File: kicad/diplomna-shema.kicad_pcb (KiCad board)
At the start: 2 copper layers, 99.8 x 79.1 mm, 20 parts, among them J1 Power input 12VDC, J7 micro switch, M2 Motor_Servo, U1 TCS3200, U2 TCRT5000, U3 HC-SR04, U4 LCD-TFT-2.8inch, U5 HX711

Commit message: Add files via upload
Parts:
- added ?: , , F.Cu at (32.6, 25.6)
- added ?: , , F.Cu at (128.4, 100.7)
- added ?: , , F.Cu at (128.4, 25.6)
- added ?: , , F.Cu at (32.6, 100.7)
- moved REF** 7.13 mm to (45.7, 99.2), turned to -90 degrees
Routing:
- net Net-(A1-Pad6): track 15.3 -> 4.42 mm
- net Net-(A1-Pad3): track 12.2 -> 3.26 mm
- net Net-(A2-Pad47): track 126.7 -> 134.1 mm
- net Net-(A2-Pad32): track 87.2 -> 94.1 mm
- net Net-(A2-Pad51): track 19.5 -> 24.7 mm
- net Net-(A1-Pad5): track 9.55 -> 4.42 mm
- net GND: track 282.4 -> 287.3 mm
- net Net-(A2-Pad45): track 154.5 -> 158.3 mm
- net +12V: track 230.8 -> 234.5 mm, vias 0 -> 1
- net Net-(A2-Pad24): track 54.7 -> 58.4 mm
- net Net-(A2-Pad37): track 68.0 -> 71.3 mm
- net Net-(A2-Pad26): track 66.4 -> 69.7 mm
- net Net-(A2-Pad35): track 45.0 -> 48.2 mm
- net Net-(A2-PadAD0): track 91.3 -> 94.3 mm
- net Net-(A1-Pad15): track 18.3 -> 21.0 mm
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- removed copper zone on F.Cu, net (none)
- removed copper zone on B.Cu, net GND
- removed copper zone on F.Cu, net GND

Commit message: Add files via upload
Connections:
- U4 pad 10: Net-(R5-Pad2) -> Net-(R3-Pad1)
- U4 pad 7: +3.3V -> Net-(R3-Pad1)
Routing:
- net +3.3V: track 98.0 -> 131.2 mm, vias 1 -> 2
- net Net-(R3-Pad1): track 81.8 -> 91.5 mm
- net Net-(A2-Pad51): track 24.7 -> 27.4 mm
- net +5V: track 216.9 -> 214.3 mm
- net +12V: track 234.5 -> 236.9 mm
- net Net-(A2-PadAD0): track 94.3 -> 92.0 mm
- net Net-(A1-Pad9): track 15.7 -> 18.0 mm
- net GND: track 287.3 -> 288.9 mm
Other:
- board text added: "T_IRG T_DO T_DIN T_CS T_CLK MISO LED SCK MOSI DC RESET CS GND VCC"

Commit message: Add files via upload
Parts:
- added R9: 10kΩ, Resistor_SMD:R_0805_2012Metric, F.Cu at (56.6, 50.9)
- moved R4 2.21 mm to (52.1, 56.8), turned to -90 degrees
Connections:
- R4 pad 1: Net-(A2-Pad39) -> GND
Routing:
- net GND: track 288.9 -> 322.1 mm, vias 2 -> 4
- net +12V: track 236.9 -> 239.0 mm, vias 1 -> 2
- net Net-(A2-Pad39): track 62.7 -> 63.3 mm

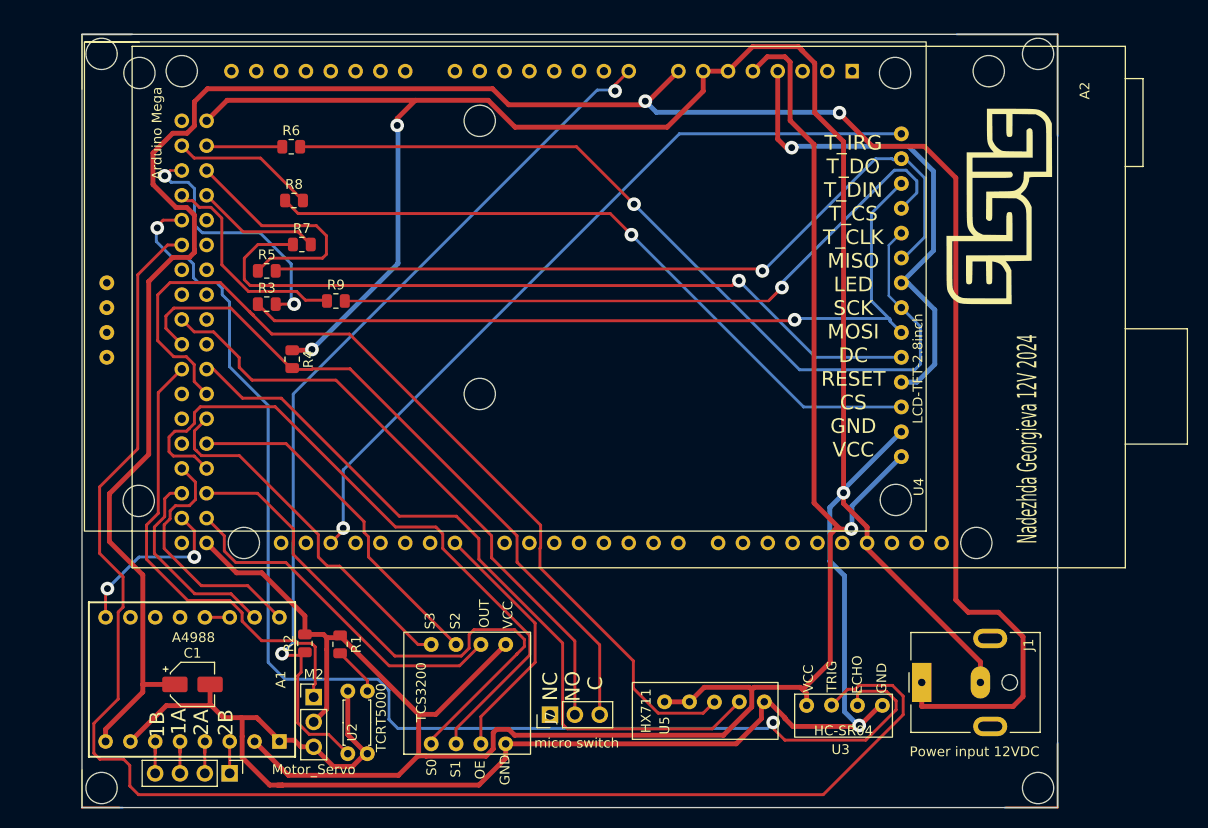
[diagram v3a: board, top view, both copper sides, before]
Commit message: последна версия - корекции по платка и схема, нови 3Dчасти за конструкция със сменен мотор и преправен код
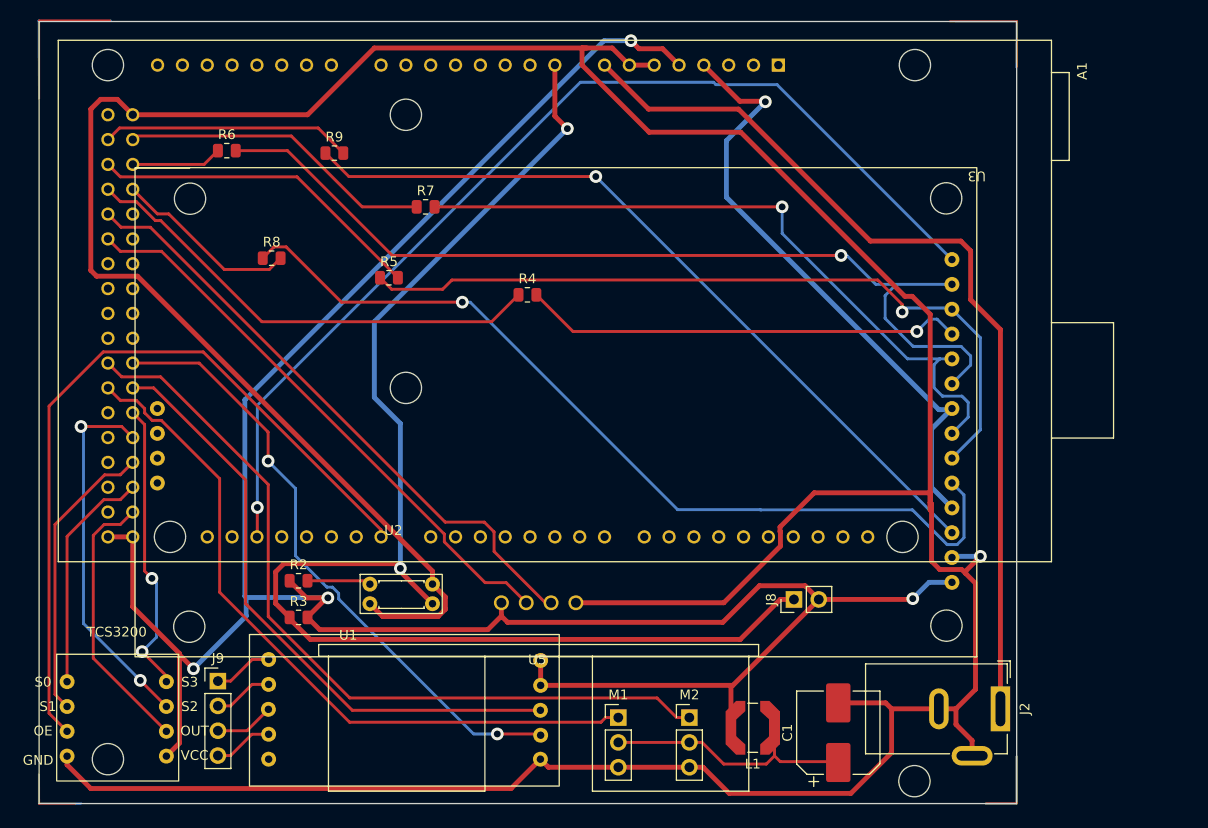
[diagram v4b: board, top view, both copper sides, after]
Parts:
- removed the ? at (32.6, 25.6)
- removed the ? at (128.4, 100.7)
- removed the ? at (128.4, 25.6)
- removed the ? at (32.6, 100.7)
- removed A2: Arduino Mega, Library:arduino_mega2560
- removed J1: Power input 12VDC, Connector_BarrelJack:BarrelJack_CUI_PJ-063AH_Horizontal
- removed J7: micro switch, Connector_PinHeader_2.54mm:PinHeader_1x03_P2.54mm_Vertical
- removed R1: 100Ω, Resistor_SMD:R_0805_2012Metric
- removed REF**: PinHeader_1x04_P2.54mm_Vertical, Connector_PinHeader_2.54mm:PinHeader_1x04_P2.54mm_Vertical
- added ?: , , F.Cu at (33.2, 97.8)
- added ?: , , F.Cu at (115.8, 100.0)
- added J2: Power input 5VDC, Connector_BarrelJack:BarrelJack_GCT_DCJ200-10-A_Horizontal, F.Cu at (124.5, 92.6)
- added J8: PinHeader_1x02_P2.54mm_Vertical, Connector_PinHeader_2.54mm:PinHeader_1x02_P2.54mm_Vertical, F.Cu at (103.4, 81.4)
- added J9: PinHeader_1x04_P2.54mm_Vertical, Connector_PinHeader_2.54mm:PinHeader_1x04_P2.54mm_Vertical, F.Cu at (44.5, 89.8)
- added L1: L, Inductor_SMD:L_Coilcraft_LPS5030, F.Cu at (99.2, 94.5)
- added M1: Motor_rampa, Connector_PinHeader_2.54mm:PinHeader_1x03_P2.54mm_Vertical, F.Cu at (85.5, 93.5)
- A1: value A4988 -> Arduino Mega; footprint Module:Pololu_Breakout-16_15.2x20.3mm -> Library:arduino_mega2560; moved to F.Cu
- C1: value C_Small -> C; footprint Capacitor_SMD:CP_Elec_4x3 -> Capacitor_SMD:CP_Elec_8x5.4
- M2: value Motor_Servo -> Futuba S3003
- R2: value 10kΩ -> 100Ω
- R4: value 10kΩ -> 10k
- U1: value TCS3200 -> HC-SR04; footprint Library:TCS3200 color sensor -> Library:XCVR_HC-SR04
- U3: value HC-SR04 -> LCD-TFT-2.8inch; footprint HC-SR04:XCVR_HC-SR04 -> Library:2.8inch_tft-lcd
- U4: value LCD-TFT-2.8inch -> TCS3200; footprint Library:2.8inch_tft-lcd -> Library:TCS3200 color sensor
- moved U3 68.1 mm to (40.9, 84.7), turned to 180 degrees
- moved U5 67.2 mm to (33.0, 82.5), turned to 0 degrees
- moved C1 66.2 mm to (108.0, 95.0), turned to 90 degrees
- moved A1 53.1 mm to (79.0, 50.9), turned to -90 degrees
- moved M2 38.5 mm to (92.7, 93.5)
- moved R3 32.2 mm to (52.8, 83.2)
- moved R4 24.9 mm to (76.2, 50.2), turned to 0 degrees
- moved U4 20.9 mm to (31.6, 92.4), turned to 0 degrees
- moved U2 18.5 mm to (62.5, 74.8), turned to 0 degrees
- moved R9 15.1 mm to (56.4, 35.8)
- moved U1 14.6 mm to (77.3, 81.8), turned to 0 degrees
- moved R7 13.2 mm to (65.8, 41.2)
- moved R5 12.5 mm to (62.0, 48.5)
- moved R6 6.60 mm to (45.4, 35.5)
- moved R2 6.43 mm to (52.8, 79.5), turned to 0 degrees
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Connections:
- A1 pad 1: GND -> unconnected-(A1-Pad1)
- A1 pad 13: Net-(A1-Pad13) -> unconnected-(A1-Pad13)
- A1 pad 14: Net-(A1-Pad13) -> Net-(U4-~{OE})
- A1 pad 15: Net-(A1-Pad15) -> unconnected-(A1-Pad15)
- A1 pad 16: Net-(A1-Pad16) -> unconnected-(A1-Pad16)
- A1 pad 2: +5V -> unconnected-(A1-Pad2)
- A1 pad 3: Net-(A1-Pad3) -> unconnected-(A1-Pad3)
- A1 pad 4: Net-(A1-Pad4) -> unconnected-(A1-Pad4)
- A1 pad 5: Net-(A1-Pad5) -> unconnected-(A1-Pad5)
- A1 pad 6: Net-(A1-Pad6) -> unconnected-(A1-Pad6)
- A1 pad 7: GND -> unconnected-(A1-Pad7)
- A1 pad 8: +12V -> unconnected-(A1-Pad8)
- A1 pad 9: Net-(A1-Pad9) -> unconnected-(A1-Pad9)
- C1 pad 1: +12V -> Net-(M1-+)
- M2 pad 1: Net-(A2-Pad35) -> Net-(M2-PWM)
- M2 pad 2: +5V -> Net-(M1-+)
- R2 pad 1: Net-(A2-PadAD0) -> +5V
- R2 pad 2: +5V -> Net-(R2-Pad2)
- R3 pad 1: Net-(R3-Pad1) -> Net-(A1-PadAD0)
- R3 pad 2: Net-(A2-Pad51) -> +5V
- R4 pad 1: GND -> Net-(A1-Pad49)
- R4 pad 2: Net-(A2-Pad37) -> Net-(U3-PIN_11)
- R5 pad 1: Net-(A2-Pad50) -> Net-(U3-PIN_12)
- R5 pad 2: Net-(R5-Pad2) -> Net-(A1-Pad51)
- R6 pad 1: Net-(A2-Pad52) -> Net-(A1-Pad50)
- R6 pad 2: +3.3V -> Net-(U3-PIN_13)
- R7 pad 1: Net-(R7-Pad1) -> Net-(A1-Pad52)
- R7 pad 2: Net-(A2-Pad48) -> Net-(U3-PIN_10)
- R8 pad 1: Net-(R8-Pad1) -> Net-(U3-PIN_5)
- R8 pad 2: Net-(A2-Pad53) -> Net-(A1-Pad48)
- R9 pad 1: Net-(A2-Pad49) -> Net-(U3-PIN_3)
- R9 pad 2: Net-(A2-Pad49) -> Net-(A1-Pad53)
- U1 pad 1: Net-(A2-Pad24) -> +5V
- U1 pad 2: Net-(A2-Pad26) -> Net-(U1-TRIG)
- U1 pad 3: Net-(A2-Pad14) -> Net-(U1-ECHO)
- U2 pad 1: Net-(R1-Pad2) -> Net-(R2-Pad2)
- U2 pad 4: Net-(A2-PadAD0) -> Net-(A1-PadAD0)
- U3 pad 2: Net-(A2-Pad45) -> GND
- U3 pad 3: Net-(A2-Pad47) -> Net-(U3-PIN_3)
- U3 pad 4: GND -> +3.3V
- U4 pad 1: +5V -> Net-(U4-S0)
- U4 pad 2: GND -> Net-(U4-S1)
- U4 pad 3: Net-(R8-Pad1) -> Net-(U4-~{OE})
- U4 pad 4: +3.3V -> GND
- U4 pad 5: Net-(R7-Pad1) -> +5V
- U4 pad 6: Net-(R3-Pad1) -> Net-(U4-OUT)
- U4 pad 7: Net-(R3-Pad1) -> Net-(U4-S2)
- U4 pad 8: +3.3V -> Net-(U4-S3)
- U5 pad 8: Net-(A2-Pad32) -> Net-(U5-PIN_8)
- U5 pad 9: Net-(A2-Pad34) -> Net-(U5-PIN_9)
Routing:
- net +12V: track 239.0 -> 0.00 mm, vias 2 -> 0
- net Net-(A2-Pad45): track 158.3 -> 0.00 mm
- net Net-(A1-PadAD0): track 0.00 -> 139.1 mm, vias 0 -> 2
- net Net-(A2-Pad47): track 134.1 -> 0.00 mm, vias 2 -> 0
- net Net-(U3-PIN_14): track 0.00 -> 105.7 mm, vias 0 -> 1
- net Net-(U3-PIN_13): track 0.00 -> 96.9 mm, vias 0 -> 1
- net Net-(A2-Pad32): track 94.0 -> 0.00 mm
- net Net-(A1-PadVIN): track 0.00 -> 93.4 mm
- net Net-(A2-Pad49): track 92.2 -> 0.00 mm, vias 1 -> 0
- net Net-(A2-PadAD0): track 92.0 -> 0.00 mm, vias 2 -> 0
- net Net-(R3-Pad1): track 91.5 -> 0.00 mm, vias 1 -> 0
- net Net-(U3-PIN_5): track 0.00 -> 91.2 mm, vias 0 -> 1
- net Net-(M2-PWM): track 0.00 -> 82.4 mm
- net Net-(R5-Pad2): track 81.6 -> 0.00 mm, vias 1 -> 0
- net Net-(U3-PIN_3): track 0.00 -> 80.2 mm, vias 0 -> 1
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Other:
- board size 99.8 x 79.1 mm -> 100 x 80 mm
- board text removed: "1A"
- board text removed: "1B"
- board text removed: "2A"
- board text removed: "2B"
- board text removed: "C"
- board text removed: "NC"
- board text removed: "NO"
- board text removed: "Nadezhda Georgieva 12V 2024"
- board text removed: "T_IRG T_DO T_DIN T_CS T_CLK MISO LED SCK MOSI DC RESET CS GND VCC"
